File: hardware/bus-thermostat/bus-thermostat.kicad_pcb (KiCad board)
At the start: 2 copper layers, 170 parts, among them J1 Screw_Terminal_01x05, J2 Screw_Terminal_01x02, J3 FTDI Serial, J4 RJ45_Shielded, M1 Fan, Q1 2N7002, Q2 2N7002, Q3 2N7002, Q4 2N7002, Q5 IRF540N, Q6 IRF540N, SW1 SW_Push, T1 PA2004NL, U1 TC652AGVUA, U10 PCA9615DP, U11 MC33660BEFR2, U12 NE555PWR, U13 TLV9301IDCK, U14 TLV9301IDCK, U15 TLV9301IDCK, U16 TLV9301IDCK, U17 TLV9301IDCK, U18 TLV9301IDCK, U19 TLV9301IDCK, U2 UCC27714D, U20 TLV9301IDCK, U21 TLV9301IDCK, U22 TLV9301IDCK, U23 74HC2G17GW-Q100H, U3 PCA9557D, U4 L7806, U5 LM7906_TO220, U6 MAX6420UK33+T, U7 NCP565D2T33R4G, U8 TLV9301IDCK, U9 ATtiny424-X

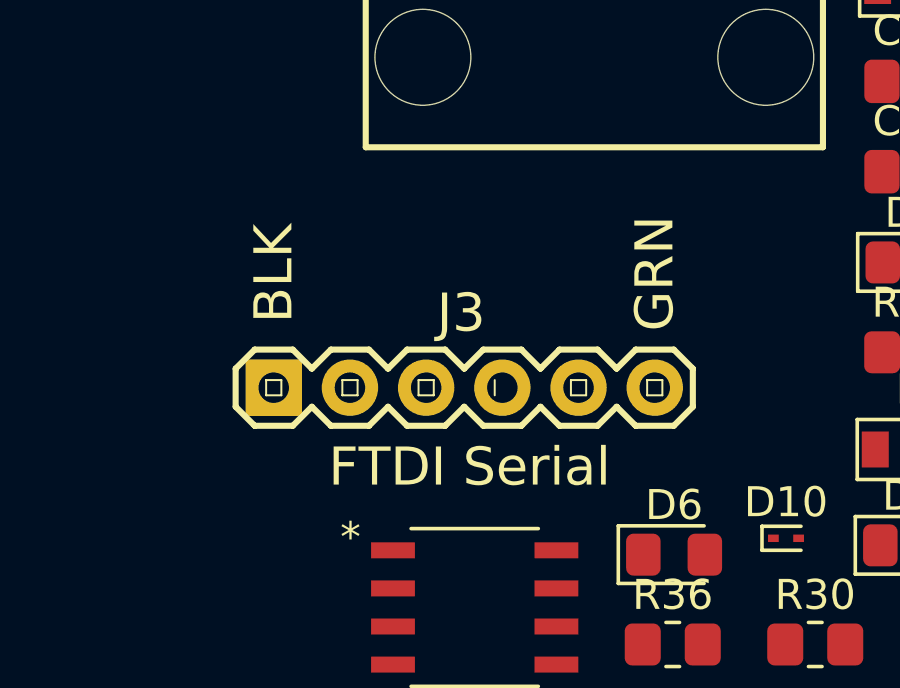
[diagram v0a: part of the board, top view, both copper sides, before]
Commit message: Added serial ports
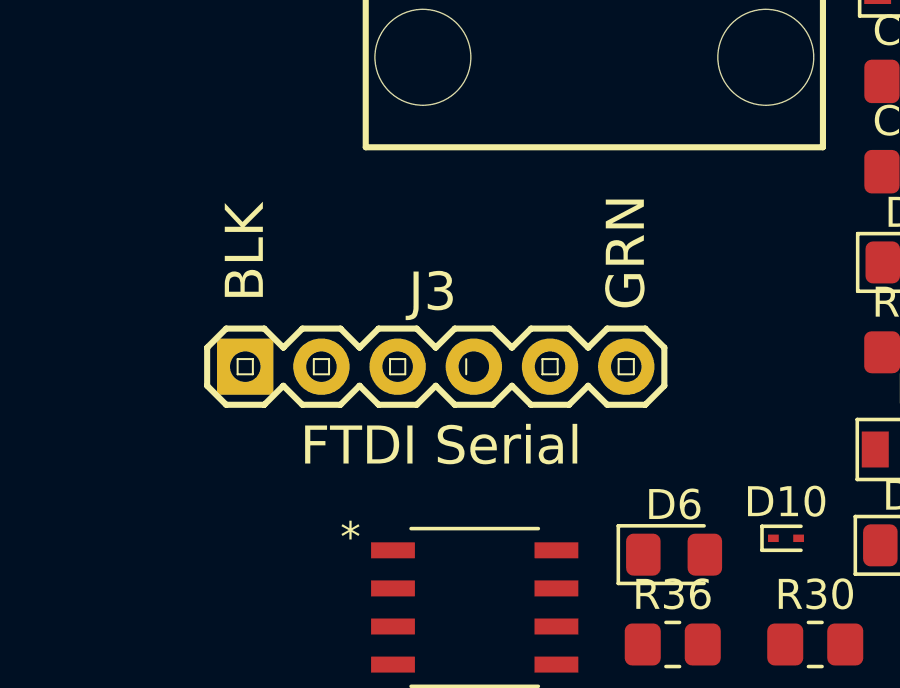
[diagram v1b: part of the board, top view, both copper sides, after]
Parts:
- moved J3 1.18 mm to (159.8, 77.5)
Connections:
- J3 pad 1: (no net) -> GND
- J3 pad 2: (no net) -> unconnected-(J3-Pad2)
- J3 pad 3: (no net) -> Net-(JP3-Pad1)
- J3 pad 4: (no net) -> Net-(R41-Pad2)
- J3 pad 5: (no net) -> UPDI
- J3 pad 6: (no net) -> unconnected-(J3-Pad6)
- JP3 pad 1: Net-(J3-PadVCC) -> Net-(JP3-Pad1)
- R20 pad 2: ~{FAN_SHDN} -> ~{TEMP_OVER}
- R22 pad 2: ~{TEMP_OVER} -> ~{FAN_SHDN}
- R41 pad 2: Net-(J3-PadTXO) -> Net-(R41-Pad2)
- U3 pad 10: ~{FAN_SHDN} -> ~{TEMP_OVER}
- U3 pad 12: ~{TEMP_OVER} -> ~{FAN_SHDN}

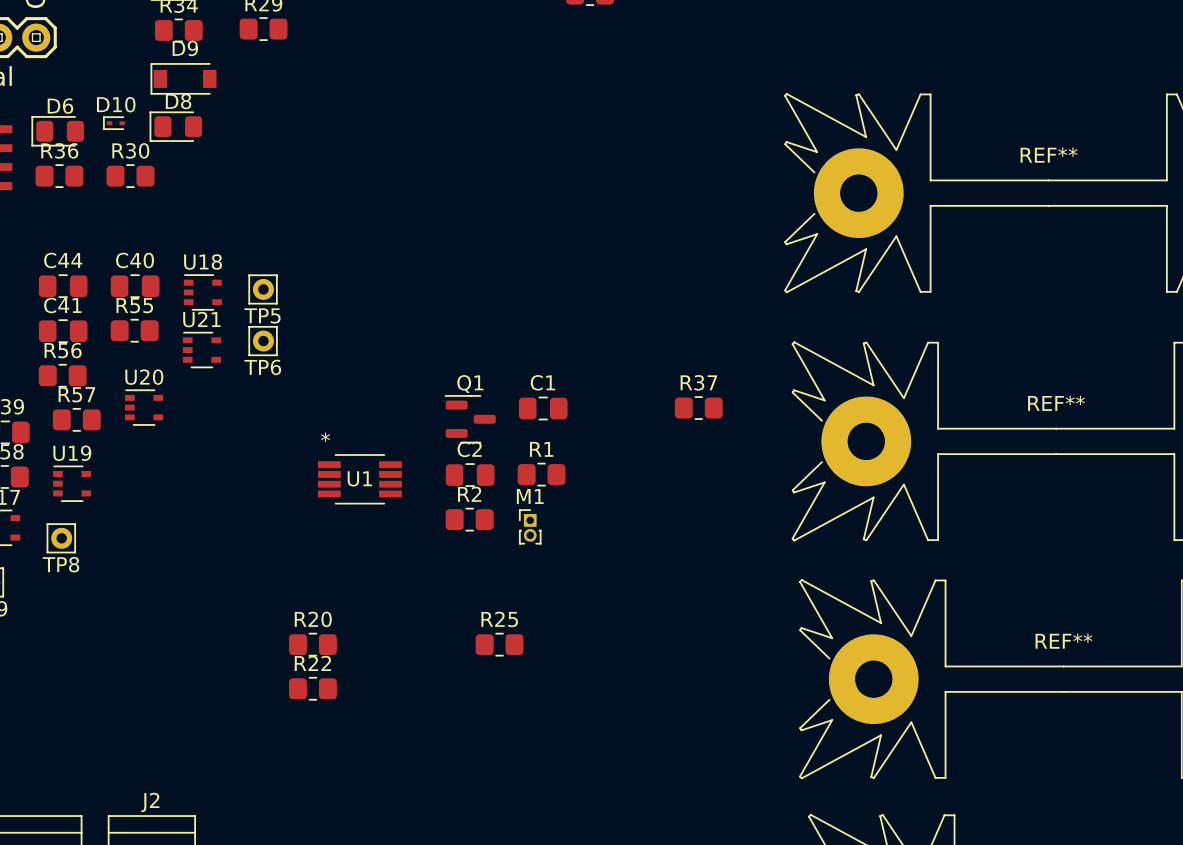
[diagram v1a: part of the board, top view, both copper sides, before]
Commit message: Misc changes, move the git libs to new repo
- https://github.com/Beirdo/KiCad-Git-Libraries
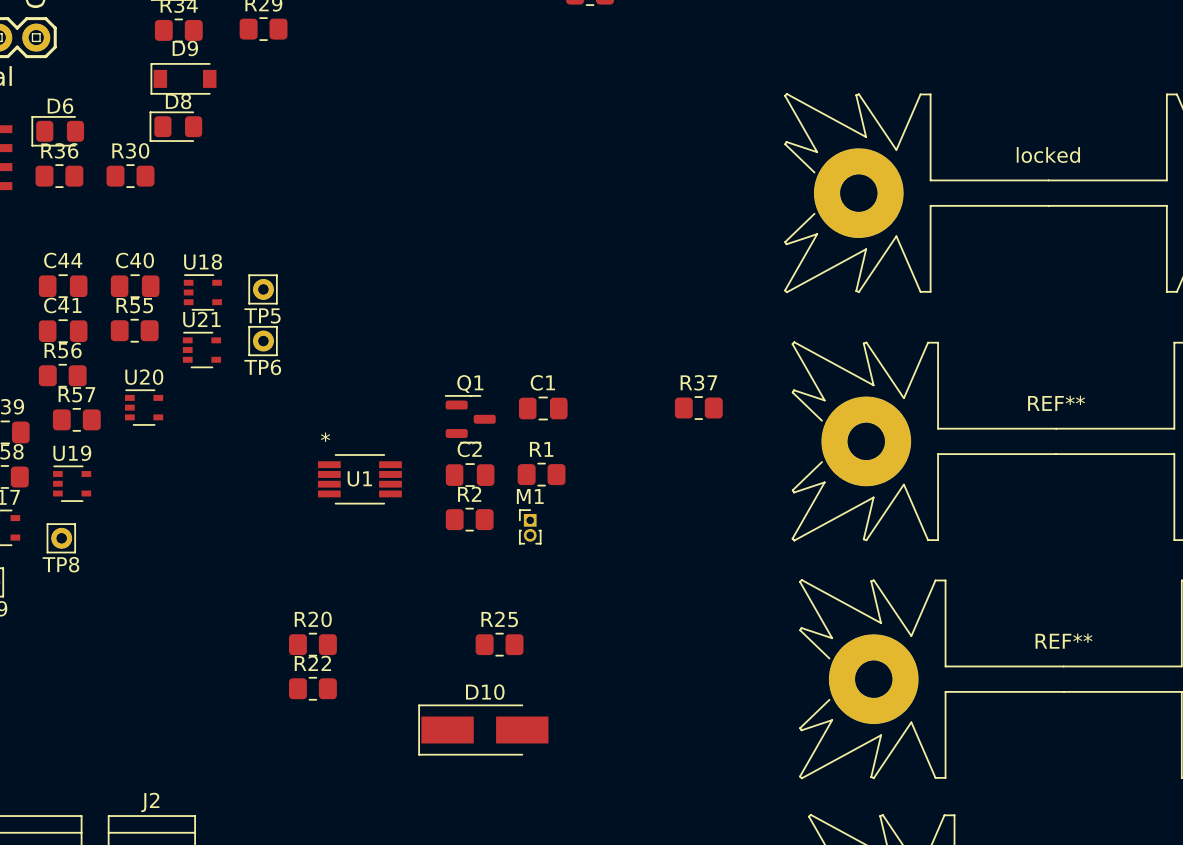
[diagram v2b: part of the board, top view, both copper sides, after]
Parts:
- D10: value ACDBQC0130L-HF -> BYS10-35; footprint Diode_SMD:D_SOD-923 -> Diode_SMD:D_SMA_Handsoldering
- moved D10 47.5 mm to (202.5, 123.8)
- renumbered REF** to locked

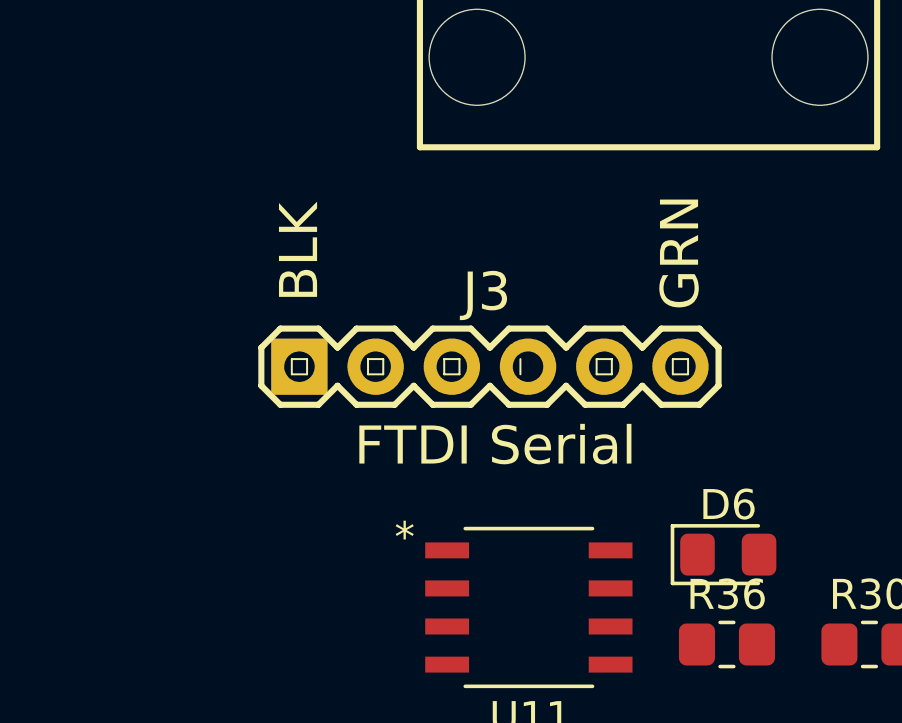
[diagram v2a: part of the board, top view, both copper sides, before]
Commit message: Moved over to PlatformIO
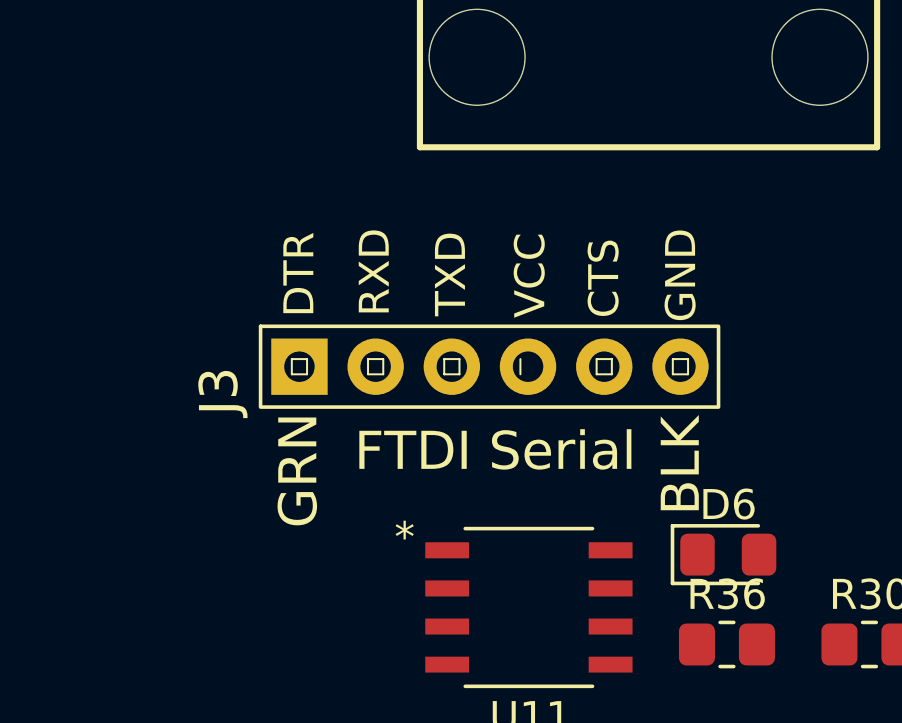
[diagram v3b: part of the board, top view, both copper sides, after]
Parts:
- J3: footprint Beirdo:FTDI_BASIC -> Beirdo:FTDI-TARGET
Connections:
- J3 pad 1: GND -> unconnected-(J3-Pad1)
- J3 pad 2: unconnected-(J3-Pad2) -> UPDI
- J3 pad 3: Net-(J3-Pad3) -> Net-(R41-Pad2)
- J3 pad 4: Net-(J3-Pad4) -> Net-(JP3-Pad1)
- J3 pad 5: UPDI -> unconnected-(J3-Pad5)
- J3 pad 6: unconnected-(J3-Pad6) -> GND
- JP3 pad 1: Net-(J3-Pad3) -> Net-(JP3-Pad1)
- R41 pad 2: Net-(J3-Pad4) -> Net-(R41-Pad2)
